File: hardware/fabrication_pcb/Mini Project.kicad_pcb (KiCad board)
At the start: 2 copper layers, 60.5 x 93.5 mm, 14 parts, among them U1 DM-OLED096-636

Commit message: feat: updated pcb layout
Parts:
- removed Speaker1: ~, MyFootprints:0.25W_8OHM_SPEAKER
- added J1: Speaker, Connector_PinHeader_2.54mm:PinHeader_1x02_P2.54mm_Vertical, B.Cu at (158.9, 44.4)
- C1, nrf1: moved to B.Cu
- moved ESP32 117.0 mm to (149.1, 135.4), turned to 90 degrees
- moved nrf1 89.6 mm to (108.7, 54.3), turned to 180 degrees
- moved C1 81.1 mm to (114.6, 62.9)
- moved MIC1 72.1 mm to (131.5, 121.8), turned to 0 degrees
- moved BTN_BACK 58.5 mm to (120.5, 82.8)
- moved BTN_SELECT 50.4 mm to (139.5, 82.8)
- moved BTN_DOWN 37.9 mm to (130.0, 90.3)
- moved BTN_UP 37.1 mm to (130.0, 75.3)
- moved U1 35.4 mm to (133.6, 56.6)
- moved amp1 31.4 mm to (153.3, 86.6), turned to 90 degrees
- moved C2 6.55 mm to (156.5, 92.5), turned to 0 degrees
- moved R1 5.70 mm to (162.1, 99.1), turned to 180 degrees
- moved R2 5.09 mm to (154.5, 103.9), turned to 0 degrees
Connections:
- C1 pad 1: VCC -> GND
- C1 pad 2: GND -> VCC
- nrf1 pad 1: VCC -> GND
- nrf1 pad 2: GND -> VCC
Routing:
- net VCC: track 122.0 -> 0.00 mm, vias 2 -> 0
- net WS: track 80.3 -> 0.00 mm
- net SCL: track 72.4 -> 0.00 mm, vias 2 -> 0
- net SDA: track 70.7 -> 0.00 mm
- net dac_out: track 55.7 -> 0.00 mm, vias 2 -> 0
- net SD: track 54.8 -> 0.00 mm
- net Net-(amp1-IN): track 54.3 -> 0.00 mm
- net Net-(ESP32-D14): track 46.5 -> 0.00 mm, vias 2 -> 0
- net MOSI: track 45.6 -> 0.00 mm
- net Net-(ESP32-D27): track 44.5 -> 0.00 mm
- net MISO: track 43.1 -> 0.00 mm
- net SCK: track 40.7 -> 0.00 mm
- net Net-(ESP32-D33): track 39.2 -> 0.00 mm
- net Net-(J1-Pin_1): track 38.7 -> 0.00 mm
- net SCK_M: track 31.4 -> 0.00 mm
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- removed copper zone on B.Cu, net GND
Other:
- board outline removed

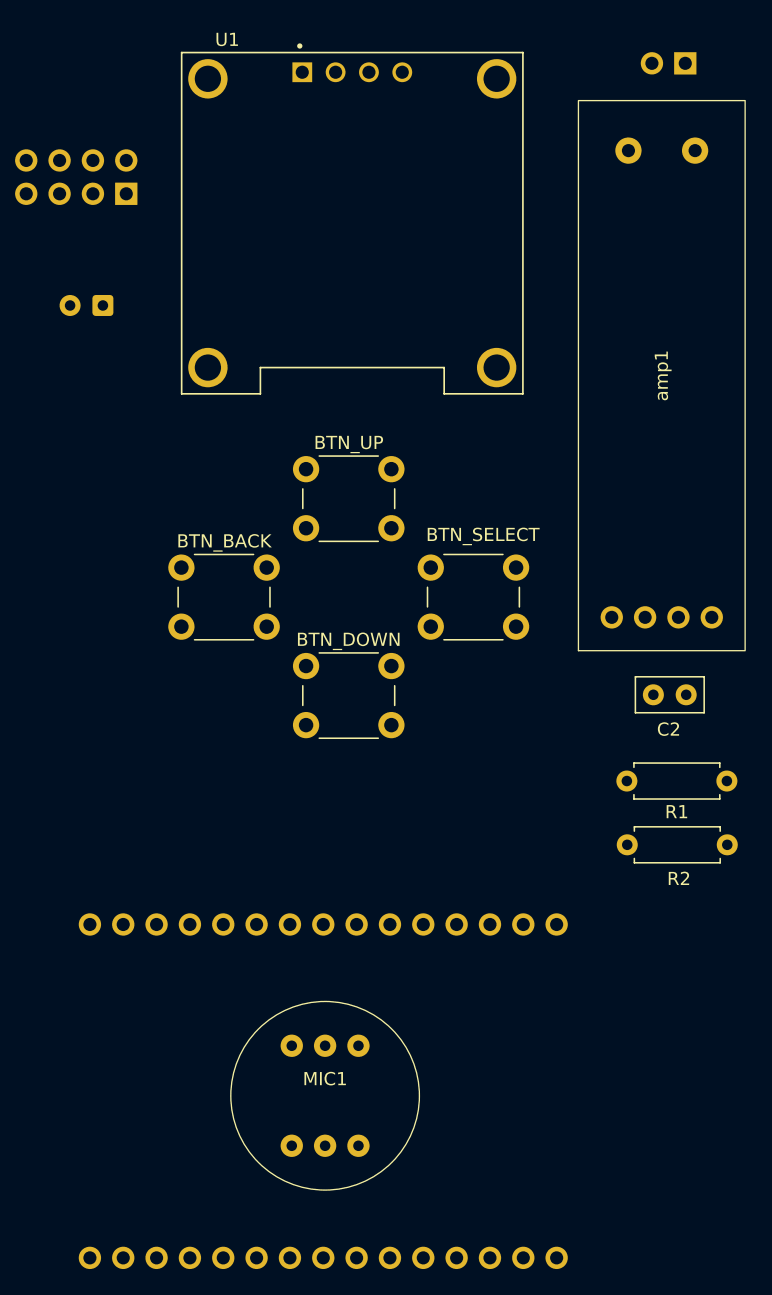
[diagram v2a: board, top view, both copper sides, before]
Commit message: fix: schematic looking fancy, component placement done
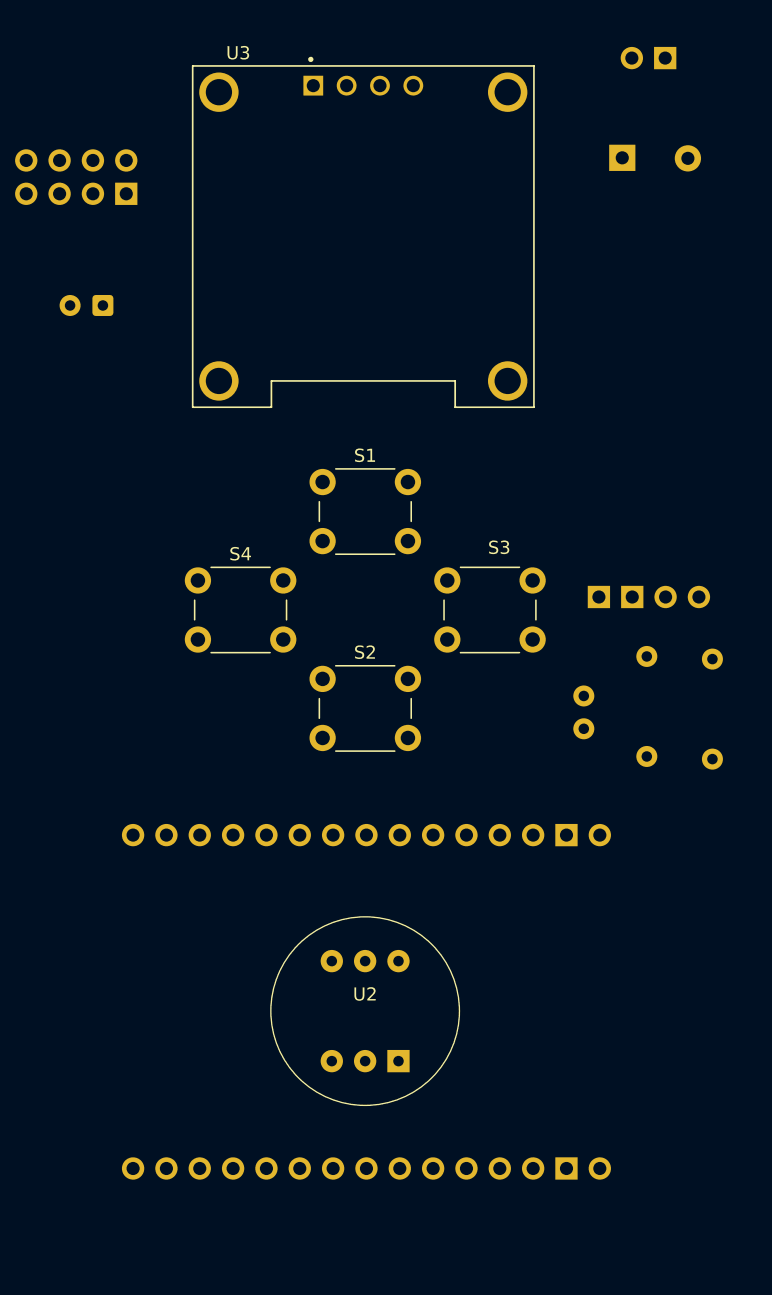
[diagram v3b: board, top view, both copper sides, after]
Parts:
- removed MIC1: ~, MyFootprints:MH-ET_I2S_MICROPHONE_MODULE
- removed amp1: ~, MyFootprints:LM386_MODULE
- added U2: MIC, MyFootprints:MH-ET_I2S_MICROPHONE_MODULE, F.Cu at (134.5, 115.3)
- added U3: OLED Display, MyFootprints:MODULE_DM-OLED096-636, F.Cu at (134.4, 57.6)
- C2, R1, R2: moved to B.Cu
- S1: renamed from BTN_UP; value SW_Push -> BTN_UP
- S2: renamed from BTN_DOWN; value SW_Push -> BTN_DOWN
- S3: renamed from BTN_SELECT; value SW_Push -> BTN_SELECT
- S4: renamed from BTN_BACK; value SW_Push -> BTN_BACK
- U1: value DM-OLED096-636 -> AMP; footprint MyFootprints:MODULE_DM-OLED096-636 -> MyFootprints:LM386_MODULE; moved to B.Cu
- moved U1 39.2 mm to (160.5, 85.1), turned to 90 degrees
- moved R2 15.6 mm to (161.0, 89.8), turned to -90 degrees
- moved ESP32 7.56 mm to (152.4, 128.6)
- moved R1 6.38 mm to (156.0, 97.2), turned to 90 degrees
- moved C2 5.90 mm to (151.2, 95.1), turned to 90 degrees
- moved S1 1.60 mm to (131.3, 76.3)
- moved S2 1.60 mm to (131.3, 91.3)
- moved S3 1.60 mm to (140.8, 83.8)
- moved S4 1.60 mm to (121.8, 83.8)
- moved J1 1.58 mm to (157.4, 44.0)
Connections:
- net Net-(ESP32-D14) renamed BTN_BACK
- net Net-(ESP32-D27) renamed BTN_SELECT
- net Net-(ESP32-D32) renamed BTN_UP
- C1 pad 1: GND -> VCC
- C1 pad 2: VCC -> GND
- C2 pad 1: Net-(amp1-IN) -> Net-(U1-IN)
- ESP32 pad 16: 5V -> unconnected-(ESP32-VIN-Pad16)
- ESP32 pad 17: unconnected-(ESP32-GND-Pad17) -> GND
- ESP32 pad 24: Net-(ESP32-D33) -> BTN_DOWN
- R1 pad 2: Net-(amp1-IN) -> Net-(U1-IN)
- R2 pad 1: Net-(amp1-IN) -> Net-(U1-IN)
- S2 pad 1: Net-(ESP32-D33) -> GND
- S2 pad 2: GND -> BTN_DOWN
- U1 pad 1: GND -> 5V
- U1 pad 2: VCC -> Net-(U1-IN)
- U1 pad 3: SCL -> GND
- U1 pad 4: SDA -> GND

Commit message: feat: routed
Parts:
- renumbered S4 to BACK, S2 to DOWN, S3 to ENTER, S1 to UP
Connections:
- net VCC renamed +3.3V
- ESP32 pad 16: unconnected-(ESP32-VIN-Pad16) -> +5V
- U1 pad 1: 5V -> +5V
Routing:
- net +3.3V: track 0.00 -> 133.6 mm
- net SDA: track 0.00 -> 111.8 mm, vias 0 -> 1
- net CE: track 0.00 -> 109.8 mm, vias 0 -> 3
- net MISO: track 0.00 -> 106.3 mm
- net CSN: track 0.00 -> 103.8 mm, vias 0 -> 1
- net SCL: track 0.00 -> 98.6 mm, vias 0 -> 2
- net SCK: track 0.00 -> 96.1 mm, vias 0 -> 2
- net MOSI: track 0.00 -> 93.9 mm
- net BTN_UP: track 0.00 -> 38.2 mm, vias 0 -> 1
- net BTN_BACK: track 0.00 -> 34.3 mm
- net dac_out: track 0.00 -> 30.8 mm
- net GND: track 0.00 -> 29.6 mm
- net BTN_SELECT: track 0.00 -> 29.0 mm, vias 0 -> 1
- net SCK_M: track 0.00 -> 21.3 mm
- net +5V: track 0.00 -> 21.3 mm
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- added copper zone on B.Cu, net GND
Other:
- board outline added: 63 x 98 mm

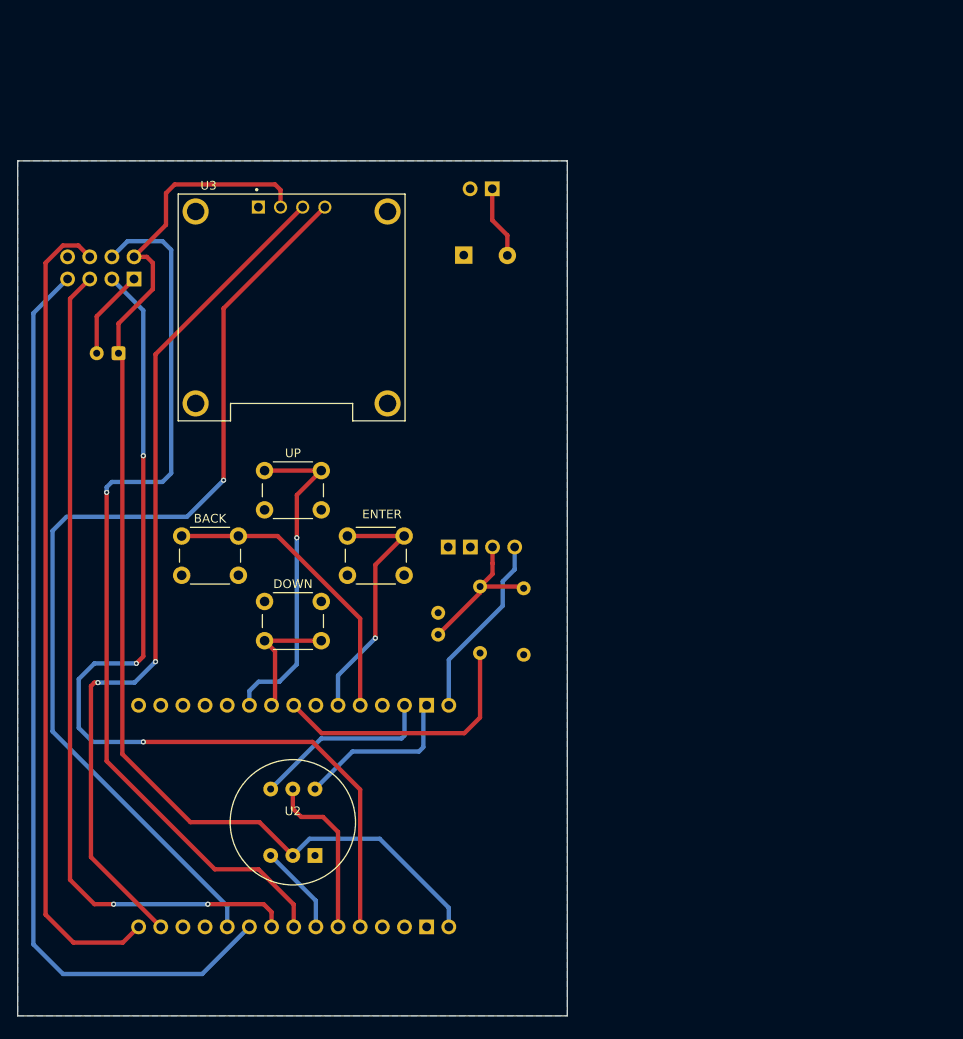
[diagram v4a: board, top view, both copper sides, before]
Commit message: feat: mount holes
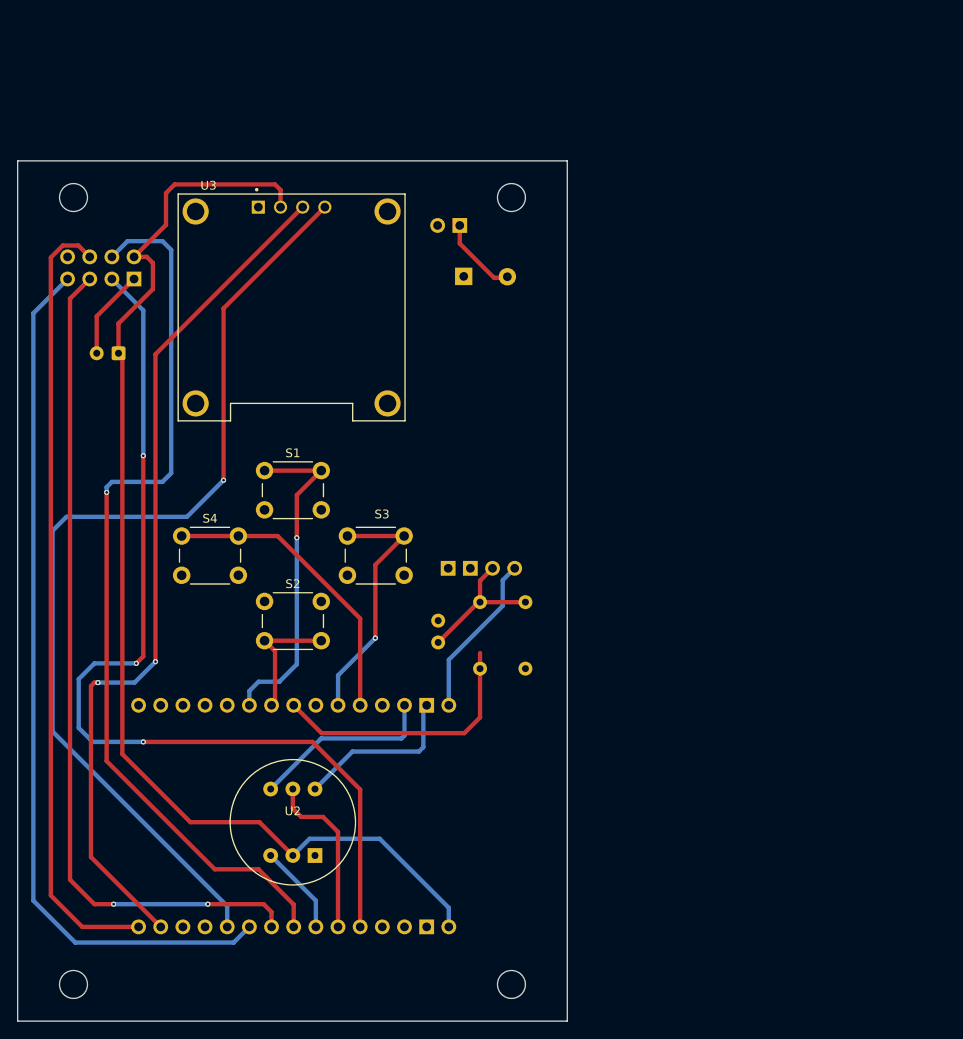
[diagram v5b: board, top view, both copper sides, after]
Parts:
- added H1: MountingHole, MountingHole:MountingHole_3.2mm_M3, F.Cu at (159.6, 45.0)
- added H2: MountingHole, MountingHole:MountingHole_3.2mm_M3, F.Cu at (109.4, 45.0)
- added H3: MountingHole, MountingHole:MountingHole_3.2mm_M3, F.Cu at (109.4, 135.2)
- added H4: MountingHole, MountingHole:MountingHole_3.2mm_M3, F.Cu at (159.6, 135.2)
- moved J1 5.61 mm to (153.7, 48.2)
- moved U1 2.44 mm to (160.5, 87.5)
- moved R1 1.79 mm to (156.0, 99.0)
- moved R2 1.60 mm to (161.2, 91.4)
- moved C2 0.90 mm to (151.2, 96.0)
- renumbered UP to S1, DOWN to S2, ENTER to S3, BACK to S4
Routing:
- net MISO: track 106.3 -> 100.4 mm
- net MOSI: track 93.9 -> 90.2 mm
- net +5V: track 21.3 -> 18.8 mm
- net Net-(U1-IN): track 17.7 -> 16.4 mm
- net Net-(J1-Pin_1): track 8.36 -> 9.21 mm
- removed copper zone on B.Cu, net GND
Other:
- board size 63 x 98 mm -> 63 x 98.6 mm

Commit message: Feat: silkscreen art
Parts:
- added C3: 47uF, Capacitor_THT:CP_Radial_D6.3mm_P2.50mm, B.Cu at (146.9, 74.4)
- added C4: 100nF, Capacitor_THT:C_Disc_D5.0mm_W2.5mm_P2.50mm, B.Cu at (146.9, 80.2)
- OLED : renamed from U3
- renumbered U1 to LM385, U2 to MIC
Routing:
- net +5V: track 18.8 -> 40.7 mm
- net dac_out: track 30.8 -> 29.0 mm
- added copper zone on B.Cu, net GND
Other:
- board text added: "Vin"
